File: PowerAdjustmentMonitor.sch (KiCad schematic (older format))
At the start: 19 parts

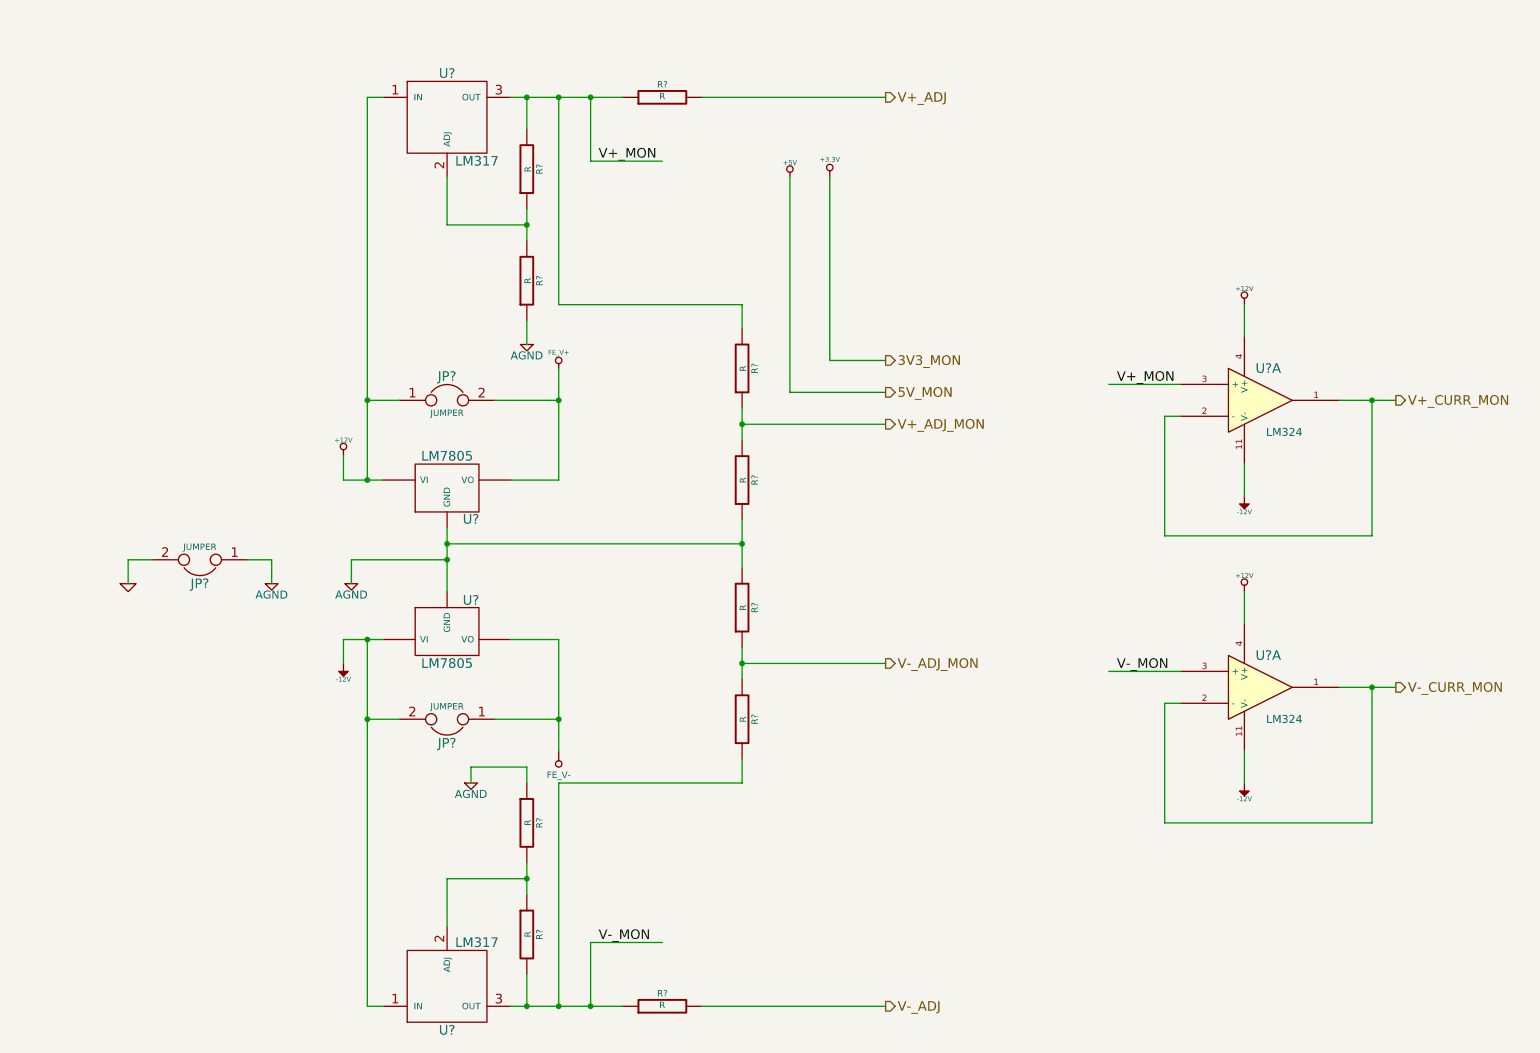
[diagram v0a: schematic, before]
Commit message: Initial layout of relay and thermocouple
All block diagrams completed through Week 3.  Component selection
spreadsheets created: Bench Buddy Session 1CE.xlsx = official part
selection and bom.xlsx is the version I came up with.

Part association and initial layout of the Relay and Thermocouple
sections completed.
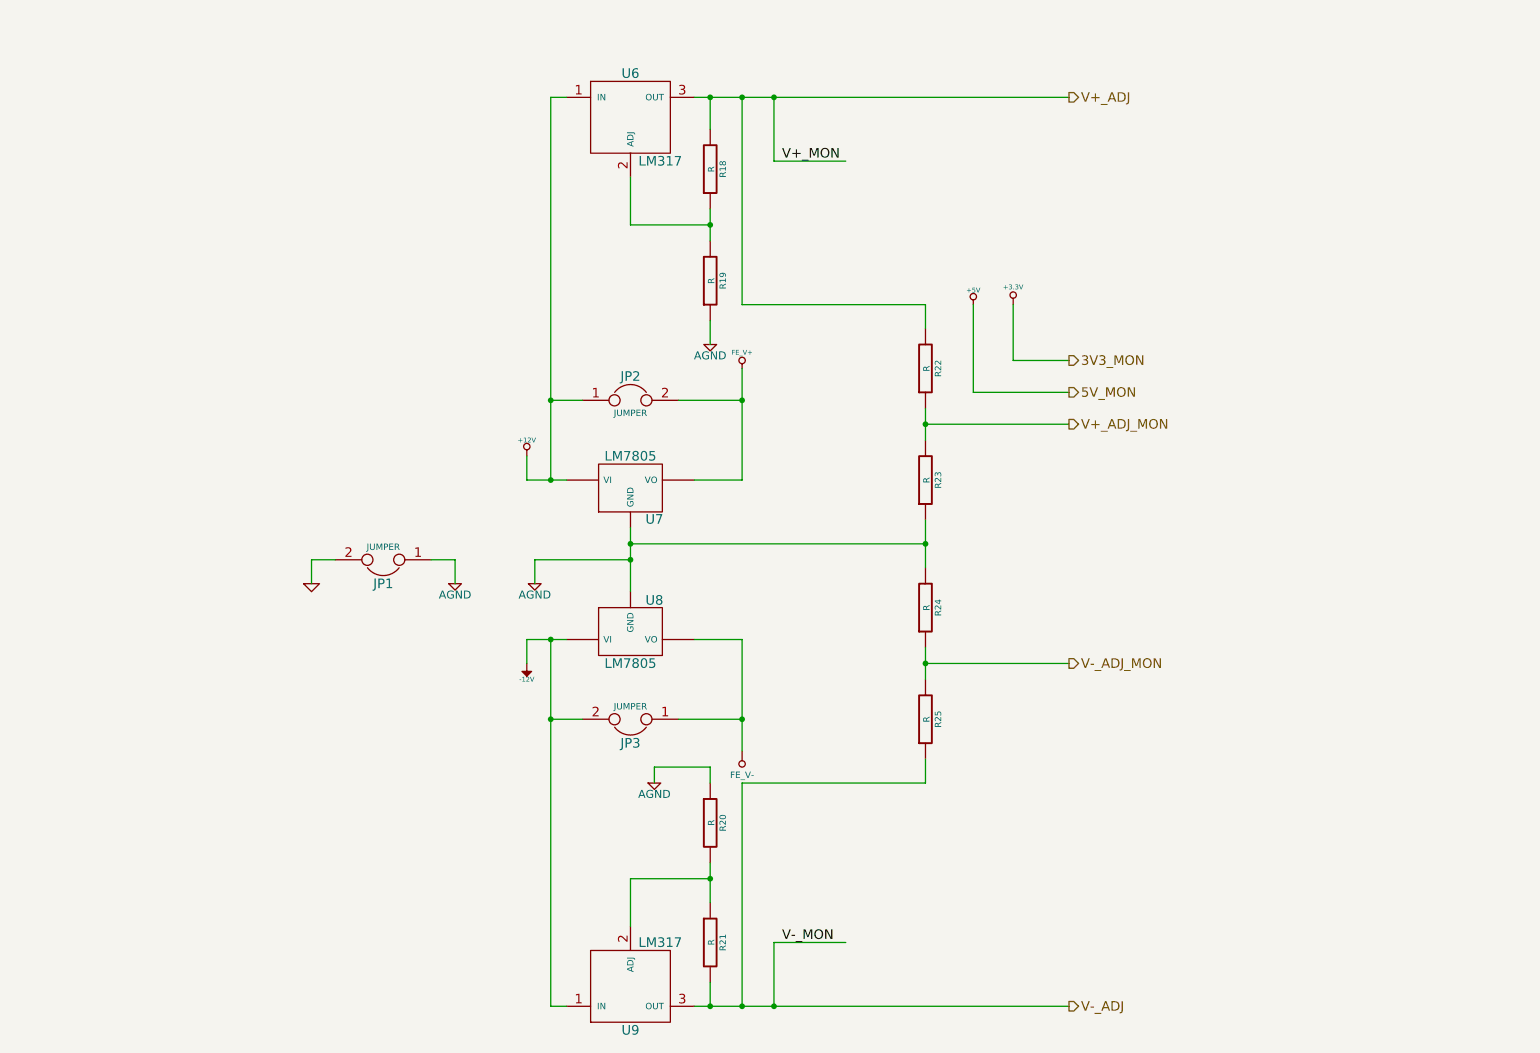
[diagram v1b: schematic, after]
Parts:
- removed R? (x2): R, ~, symbol R
- removed U? (x2): LM324, symbol LM324
- gave numbers to parts that had none: 15
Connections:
- net labels removed: V+_CURR_MON, V-_CURR_MON
- wire segments 96 -> 76
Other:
- moved on the sheet: JP1, JP2, JP3, R18, R19, R20, R21, R22, R23, R24, R25, U6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

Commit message: Initial layout of Arduino and Fan-Current
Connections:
- wire segments 76 -> 57
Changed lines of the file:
@@
 Sheet 6 9
 Title ""
-Date "21 feb 2014"
+Date "22 feb 2014"
 Rev ""
 Comp ""
@@
 $EndComp
 Wire Wire Line
-	3850 3600 4000 3600
-Wire Wire Line
-	4000 3600 4100 3600
+	3850 3600 4100 3600
 Wire Wire Line
 	3850 4750 3850 4600
 Wire Wire Line
-	3850 4600 4000 4600
-Wire Wire Line
-	4000 4600 4100 4600
+	3850 4600 4100 4600
 $Comp
 L JUMPER JP2
@@
 $EndComp
 Wire Wire Line
-	4000 4600 4000 5100
-Wire Wire Line
-	4000 5100 4000 6900
+	4000 4600 4000 6900
 Wire Wire Line
 	4000 5100 4200 5100
@@
 	4200 3100 4000 3100
 Wire Wire Line
-	4000 1200 4000 3100
-Wire Wire Line
-	4000 3100 4000 3600
+	4000 1200 4000 3600
 Connection ~ 4000 3600
 Wire Wire Line
 	4800 3100 5200 3100
 Wire Wire Line
-	5200 2900 5200 3100
-Wire Wire Line
-	5200 3100 5200 3600
+	5200 2900 5200 3600
 Wire Wire Line
 	5200 3600 4900 3600
@@
 $EndComp
 Wire Wire Line
-	4500 3900 4500 4000
-Wire Wire Line
-	4500 4000 4500 4100
-Wire Wire Line
-	4500 4100 4500 4300
+	4500 3900 4500 4300
 Wire Wire Line
 	3900 4100 4500 4100
@@
 	5000 6900 5000 6750
 Wire Wire Line
-	5000 6000 5000 6100
-Wire Wire Line
-	5000 6100 5000 6250
+	5000 6000 5000 6250
 Wire Wire Line
 	5000 6100 4500 6100
@@
 	5000 1200 5000 1400
 Wire Wire Line
-	6350 3150 6350 3250
-Wire Wire Line
-	6350 3250 6350 3350
+	6350 3150 6350 3350
 Wire Wire Line
 	4500 2000 4500 1700
@@
 $EndComp
 Wire Wire Line
-	5200 4600 5200 5100
-Wire Wire Line
-	5200 5100 5200 5300
+	5200 4600 5200 5300
 Connection ~ 5200 5100
 Wire Wire Line
@@
 $EndComp
 Wire Wire Line
-	6350 4650 6350 4750
-Wire Wire Line
-	6350 4750 6350 4850
+	6350 4650 6350 4850
 Wire Wire Line
 	6350 5350 6350 5500
 Wire Wire Line
-	6350 3850 6350 4000
-Wire Wire Line
-	6350 4000 6350 4150
+	6350 3850 6350 4150
 Connection ~ 6350 4000
 Wire Wire Line
@@
 $EndComp
 Wire Wire Line
-	5000 1900 5000 2000
-Wire Wire Line
-	5000 2000 5000 2100
+	5000 1900 5000 2100
 Wire Wire Line
 	5000 2000 4500 2000
@@
 	6650 3050 7250 3050
 Wire Wire Line
-	4900 6900 5000 6900
-Wire Wire Line
-	5000 6900 5200 6900
-Wire Wire Line
-	5200 6900 5400 6900
-Wire Wire Line
-	5400 6900 7250 6900
-Wire Wire Line
-	4900 1200 5000 1200
-Wire Wire Line
-	5000 1200 5200 1200
-Wire Wire Line
-	5200 1200 5400 1200
-Wire Wire Line
-	5400 1200 7250 1200
+	4900 6900 7250 6900
+Wire Wire Line
+	4900 1200 7250 1200
 Text Label 5450 6500 0    60   ~ 0
 V-_MON

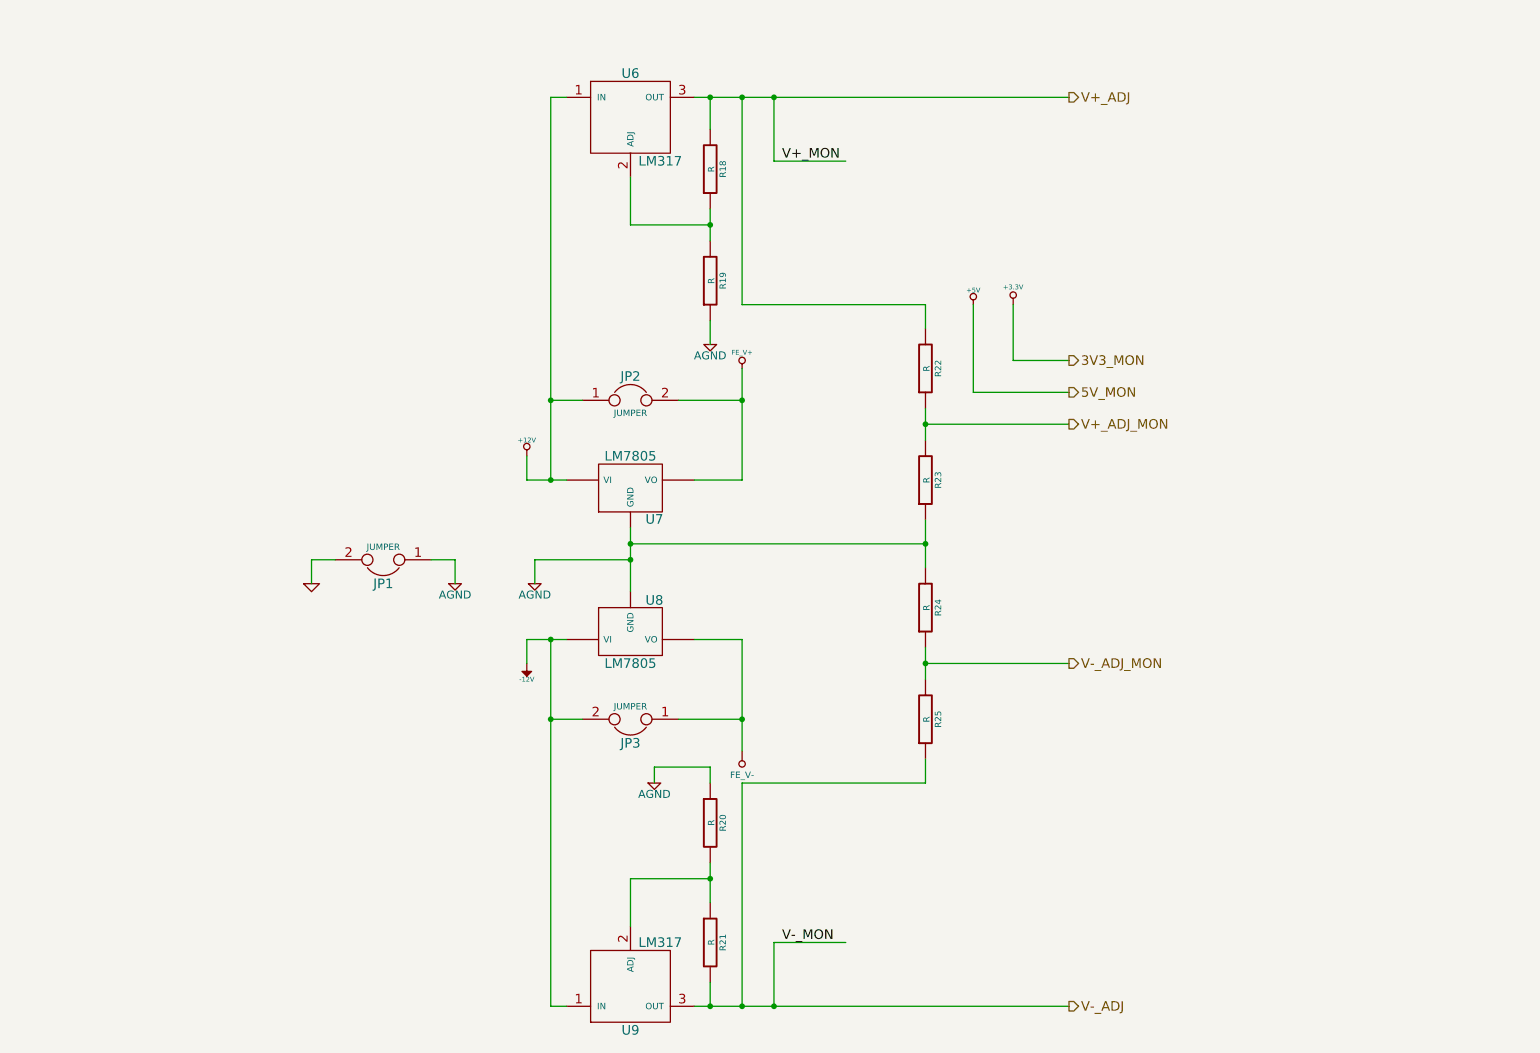
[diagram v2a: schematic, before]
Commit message: Reorganization of power conditioning module
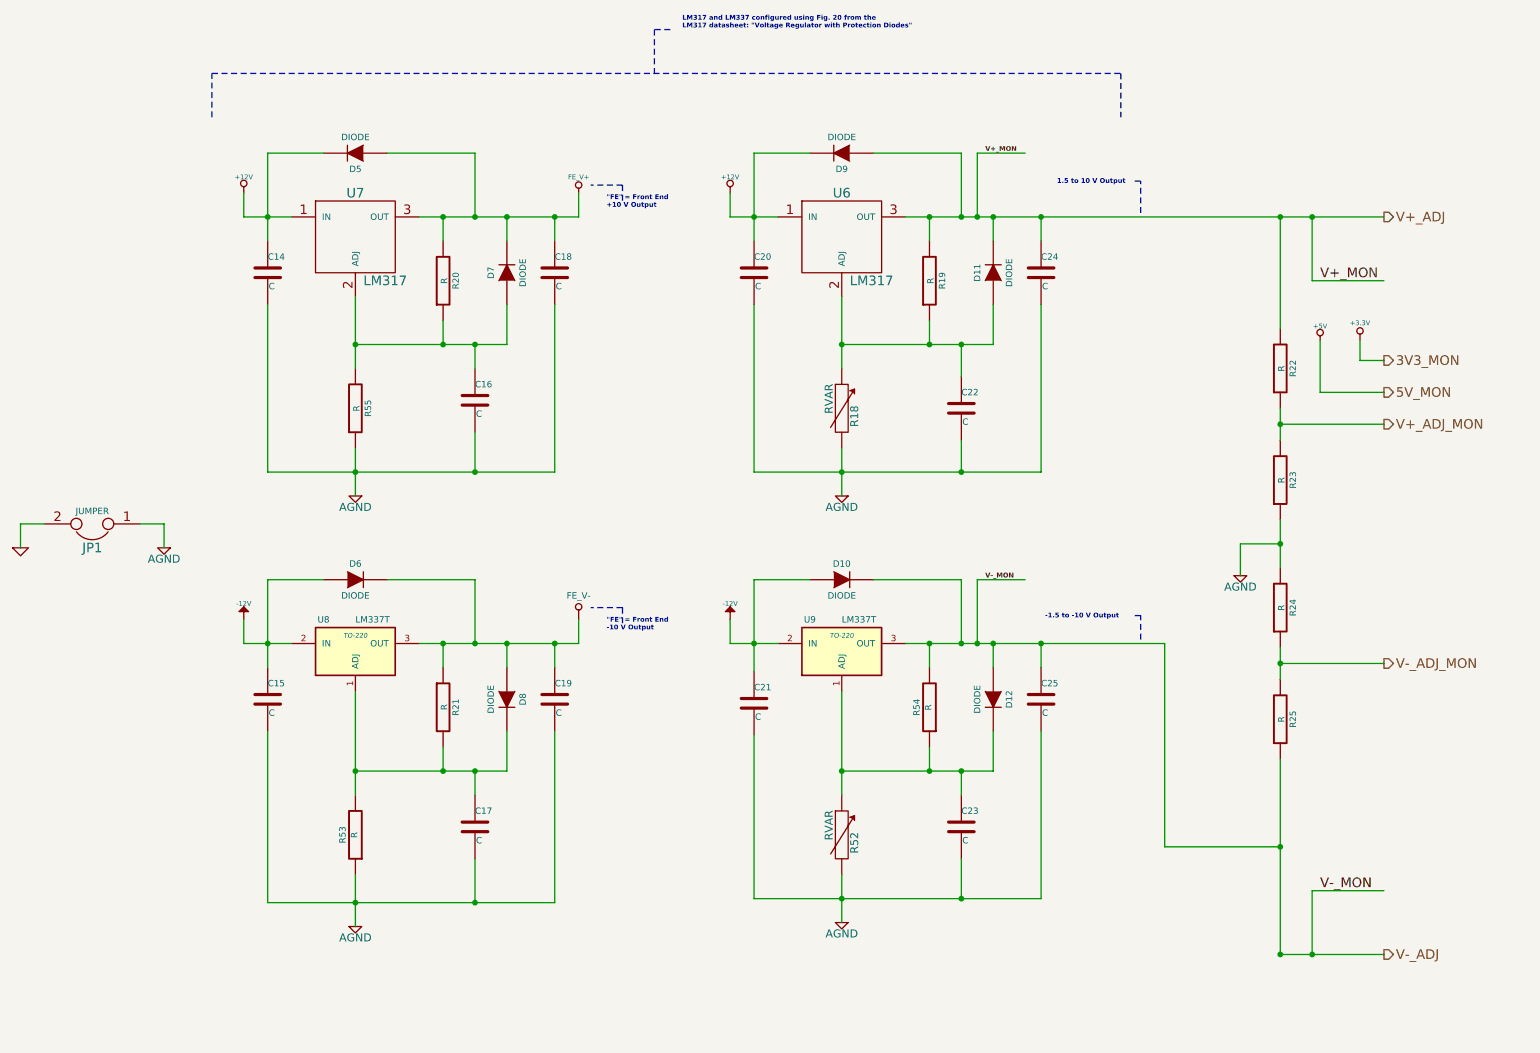
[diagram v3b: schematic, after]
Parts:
- removed JP2, JP3: JUMPER, ~, symbol JUMPER
- removed R18: R, ~, symbol R
- removed U7, U8: LM7805, ~, symbol LM7805
- removed U9: LM317, ~, symbol LM317
- added C14, C15, C16, C17, C18, C19, C20, C21, C22, C23, C24, C25: C, ~, symbol C
- added D10, D11, D12, D5, D6, D7, D8, D9: DIODE, ~, symbol DIODE
- added R18, R52: RVAR, ~, symbol RVAR
- added R53, R54, R55: R, ~, symbol R
- added U7: LM317, ~, symbol LM317
- added U8, U9: LM337T, TO-220, symbol LM337T
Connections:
- wire segments 57 -> 110
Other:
- note added: ""FE" = Front End\n+10 V Output"
- note added: ""FE" = Front End\n-10 V Output"
- note added: "-1.5 to -10 V Output"
- note added: "1.5 to 10 V Output"
- note added: "LM317 and LM337 configured using Fig. 20 from the \nLM317 datasheet: "Voltage Regulator with Protection Diodes""
- moved on the sheet: JP1, R19, R22, R23, R24, R25, U6
